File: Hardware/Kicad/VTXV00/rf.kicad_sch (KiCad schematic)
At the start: 48 parts, among them J2 U.FL, U3 RTC6705, U4 RFPA5542, Y1 8MHz 12pF

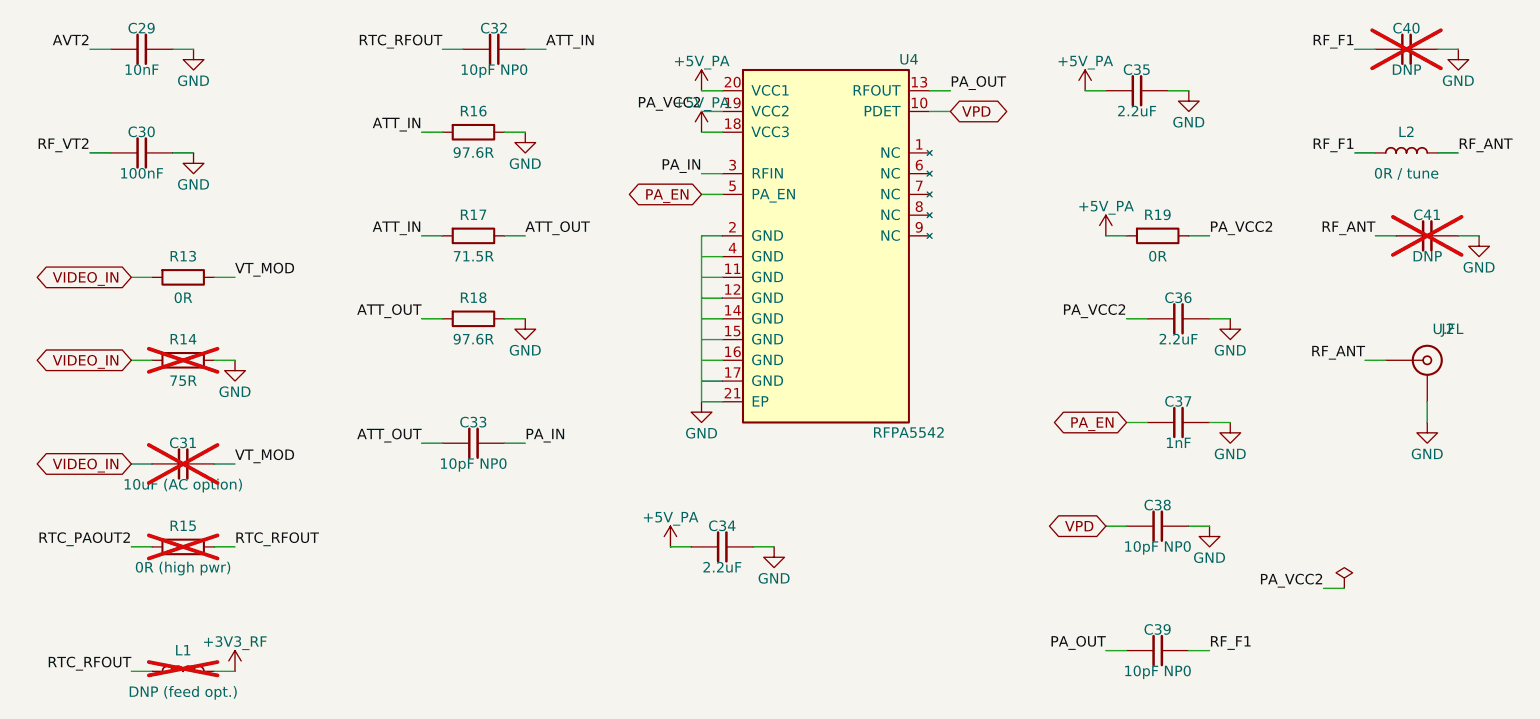
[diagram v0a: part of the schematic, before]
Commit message: Upgrade to KiCad 10 and use shared Kicad_Libs only
- Upgrade ESCV00, FCV00, RXV00, VTXV00 schematics and PCBs to KiCad 10
- Remove KiCad_Libs_Drone and merge_libs (parts already in Kicad_Libs)
- Lib tables list every Kicad_Libs library
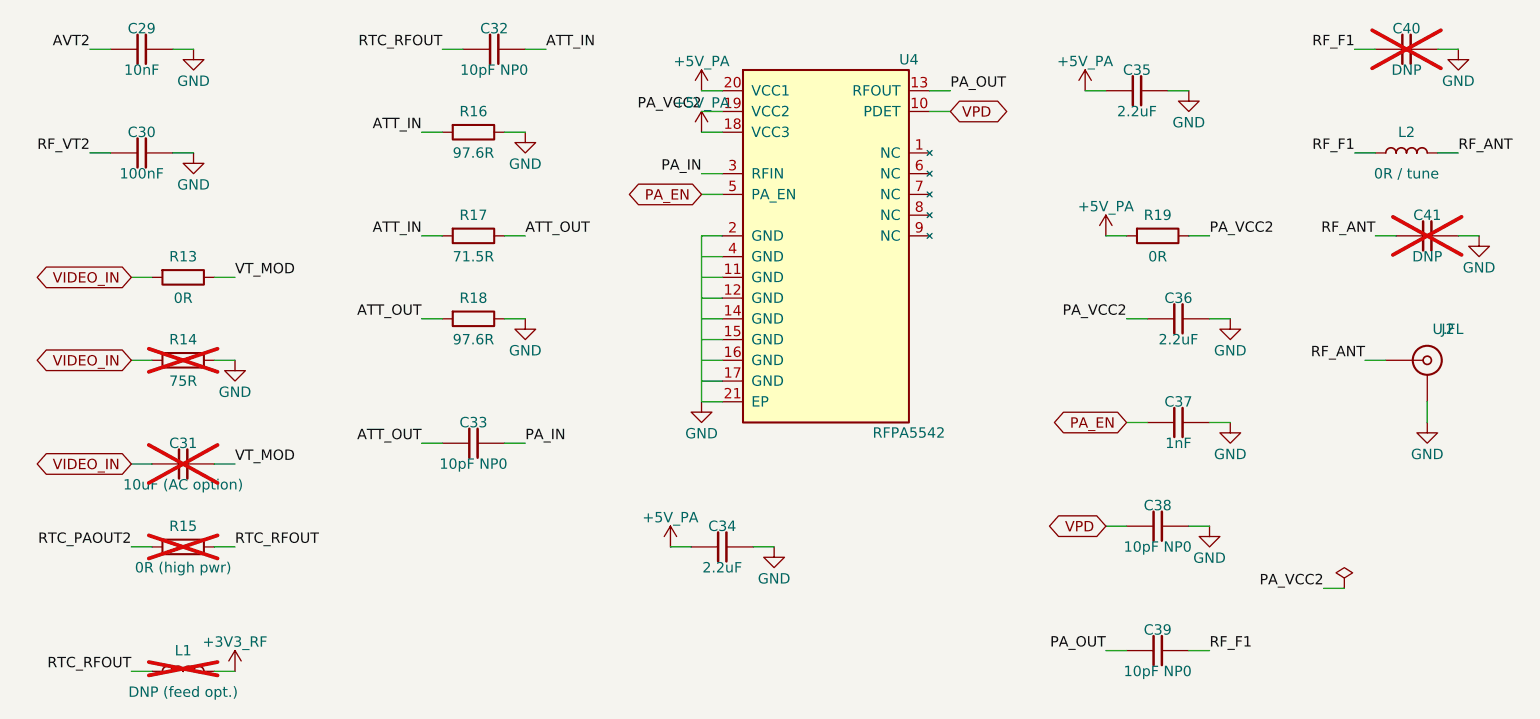
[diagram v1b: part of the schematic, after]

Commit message: Boards follow the B0_EE part convention
- every real part uses the symbol/footprint/3D/datasheet named after its MPN in Kicad_Libs
- symbols keep only Reference, Value, Footprint, Datasheet, Description
  (MPN, Manufacturer, Verify, LCSC, Note fields removed; Verify notes moved to the Readme)
- schematic symbol caches rebuilt from the libraries, PCB footprints relinked with the
  same fields and 3D models as the library (connectivity unchanged)
- DNP and BOM attributes of the footprints match the symbols
- BOMs re-exported with kicad-cli
- ignore KiCad local history
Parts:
- FB2: value 120R@100MHz -> BLM18PG121SN1D; footprint eChoke:L_0603_1608Metric -> eFerrite:BLM18PG121SN1D; symbol eChoke:FB -> eFerrite:BLM18PG121SN1D; MPN BLM18PG121SN1D -> (none)
- J2: value U.FL -> U.FL-R-SMT-1; footprint eConnector:U.FL_Hirose_U.FL-R-SMT-1_Vertical -> eConnector:U.FL-R-SMT-1; symbol eConnector:Conn_Coaxial -> eConnector:U.FL-R-SMT-1; MPN U.FL-R-SMT-1(10) -> (none); Manufacturer Hirose -> (none)
- U3: footprint eRFModule:QFN-40-1EP_6x6mm_P0.5mm_EP4.6x4.6mm -> eRFModule:RTC6705; MPN RTC6705 -> (none); Manufacturer RichWave -> (none); Verify Pin table from RichWave RTC6705 datasheet V0.2 (datasheet/R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 -> (none)
- U4: value RFPA5542 -> RFPA5542TR13; footprint eAmplifier:QFN-20-1EP_4x4mm_P0.5mm_EP2.5x2.5mm -> eAmplifier:RFPA5542TR13; symbol eAmplifier:RFPA5542 -> eAmplifier:RFPA5542TR13; MPN RFPA5542TR13 -> (none); Manufacturer Qorvo -> (none)
- Y1: value 8MHz 12pF -> X322508MLB4SI; footprint eCrystal:Crystal_SMD_3225-4Pin_3.2x2.5mm -> eCrystal:X322508MLB4SI; symbol eCrystal:Crystal_GND24 -> eCrystal:X322508MLB4SI; MPN X322508MLB4SI -> (none); Manufacturer Yangxing -> (none)

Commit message: Cleared all the descriptions and started Power section for FCV
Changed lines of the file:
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@@
 			(show_name no)
 			(do_not_autoplace no)
+			(hide yes)
 			(effects
 				(font
@@
 			(show_name no)
 			(do_not_autoplace no)
+			(hide yes)
 			(effects
 				(font
@@
 			(show_name no)
 			(do_not_autoplace no)
+			(hide yes)
 			(effects
 				(font
@@
 			(show_name no)
 			(do_not_autoplace no)
+			(hide yes)
 			(effects
 				(font
@@
 			(show_name no)
 			(do_not_autoplace no)
+			(hide yes)
 			(effects
 				(font
@@
 			(show_name no)
 			(do_not_autoplace no)
+			(hide yes)
 			(effects
 				(font
@@
 			(show_name no)
 			(do_not_autoplace no)
+			(hide yes)
 			(effects
 				(font
@@
 			(show_name no)
 			(do_not_autoplace no)
+			(hide yes)
 			(effects
 				(font
@@
 			(show_name no)
 			(do_not_autoplace no)
+			(hide yes)
 			(effects
 				(font
@@
 			(show_name no)
 			(do_not_autoplace no)
+			(hide yes)
 			(effects
 				(font
@@
 			(show_name no)
 			(do_not_autoplace no)
+			(hide yes)
 			(effects
 				(font
@@
 			(show_name no)
 			(do_not_autoplace no)
+			(hide yes)
 			(effects
 				(font
@@
 			(show_name no)
 			(do_not_autoplace no)
+			(hide yes)
 			(effects
 				(font
@@
 			(show_name no)
 			(do_not_autoplace no)
+			(hide yes)
 			(effects
 				(font
@@
 			(show_name no)
 			(do_not_autoplace no)
+			(hide yes)
 			(effects
 				(font
@@
 			(show_name no)
 			(do_not_autoplace no)
+			(hide yes)
 			(effects
 				(font
@@
 			(show_name no)
 			(do_not_autoplace no)
+			(hide yes)
 			(effects
 				(font
@@
 			(show_name no)
 			(do_not_autoplace no)
+			(hide yes)
 			(effects
 				(font
@@
 			(show_name no)
 			(do_not_autoplace no)
+			(hide yes)
 			(effects
 				(font
@@
 			(show_name no)
 			(do_not_autoplace no)
+			(hide yes)
 			(effects
 				(font
@@
 			(show_name no)
 			(do_not_autoplace no)
+			(hide yes)
 			(effects
 				(font
@@
 			(show_name no)
 			(do_not_autoplace no)
+			(hide yes)
 			(effects
 				(font
@@
 			(show_name no)
 			(do_not_autoplace no)
+			(hide yes)
 			(effects
 				(font
@@
 			(show_name no)
 			(do_not_autoplace no)
+			(hide yes)
 			(effects
 				(font
@@
 			(show_name no)
 			(do_not_autoplace no)
+			(hide yes)
 			(effects
 				(font
@@
 			(show_name no)
 			(do_not_autoplace no)
+			(hide yes)
 			(effects
 				(font
@@
 			(show_name no)
 			(do_not_autoplace no)
+			(hide yes)
 			(effects
 				(font
@@
 			(show_name no)
 			(do_not_autoplace no)
+			(hide yes)
 			(effects
 				(font
@@
 			(show_name no)
 			(do_not_autoplace no)
+			(hide yes)
 			(effects
 				(font
@@
 			(show_name no)
 			(do_not_autoplace no)
+			(hide yes)
 			(effects
 				(font
@@
 			(show_name no)
 			(do_not_autoplace no)
+			(hide yes)
 			(effects
 				(font
@@
 			(show_name no)
 			(do_not_autoplace no)
+			(hide yes)
 			(effects
 				(font
@@
 			(show_name no)
 			(do_not_autoplace no)
+			(hide yes)
 			(effects
 				(font
@@
 			(show_name no)
 			(do_not_autoplace no)
+			(hide yes)
 			(effects
 				(font
@@
 			(show_name no)
 			(do_not_autoplace no)
+			(hide yes)
 			(effects
 				(font
@@
 			(show_name no)
 			(do_not_autoplace no)
+			(hide yes)
 			(effects
 				(font
@@
 			(show_name no)
 			(do_not_autoplace no)
+			(hide yes)
 			(effects
 				(font
@@
 			(show_name no)
 			(do_not_autoplace no)
+			(hide yes)
 			(effects
 				(font
@@
 			(show_name no)
 			(do_not_autoplace no)
+			(hide yes)
 			(effects
 				(font
@@
 			(show_name no)
 			(do_not_autoplace no)
+			(hide yes)
 			(effects
 				(font
@@
 			(show_name no)
 			(do_not_autoplace no)
+			(hide yes)
 			(effects
 				(font
@@
 			(show_name no)
 			(do_not_autoplace no)
+			(hide yes)
 			(effects
 				(font
@@
 			(show_name no)
 			(do_not_autoplace no)
+			(hide yes)
 			(effects
 				(font
@@
 			(show_name no)
 			(do_not_autoplace no)
+			(hide yes)
 			(effects
 				(font
@@
 			(show_name no)
 			(do_not_autoplace no)
+			(hide yes)
 			(effects
 				(font
@@
 			(show_name no)
 			(do_not_autoplace no)
+			(hide yes)
 			(effects
 				(font
@@
 			(show_name no)
 			(do_not_autoplace no)
+			(hide yes)
 			(effects
 				(font
@@
 			(show_name no)
 			(do_not_autoplace no)
+			(hide yes)
 			(effects
 				(font
@@
 			(show_name no)
 			(do_not_autoplace no)
+			(hide yes)
 			(effects
 				(font
@@
 			(show_name no)
 			(do_not_autoplace no)
+			(hide yes)
 			(effects
 				(font
@@
 			(show_name no)
 			(do_not_autoplace no)
+			(hide yes)
 			(effects
 				(font
@@
 			(show_name no)
 			(do_not_autoplace no)
+			(hide yes)
 			(effects
 				(font
@@
 			(show_name no)
 			(do_not_autoplace no)
+			(hide yes)
 			(effects
 				(font
@@
 			(show_name no)
 			(do_not_autoplace no)
+			(hide yes)
 			(effects
 				(font
@@
 			(show_name no)
 			(do_not_autoplace no)
+			(hide yes)
 			(effects
 				(font
@@
 			(show_name no)
 			(do_not_autoplace no)
+			(hide yes)
 			(effects
 				(font
@@
 			(show_name no)
 			(do_not_autoplace no)
+			(hide yes)
 			(effects
 				(font
@@
 			(show_name no)
 			(do_not_autoplace no)
+			(hide yes)
 			(effects
 				(font
@@
 			(show_name no)
 			(do_not_autoplace no)
+			(hide yes)
 			(effects
 				(font
@@
 			(show_name no)
 			(do_not_autoplace no)
+			(hide yes)
 			(effects
 				(font
